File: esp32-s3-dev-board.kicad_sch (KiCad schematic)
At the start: 16 parts, among them IC1 ESP32-S3-WROOM-1-N8R8, J1 Conn_01x18, J2 Conn_01x18, J3 PROG_HDR, Q1 SS8050-G, Q2 SS8050-G, SW1 SW_Reset

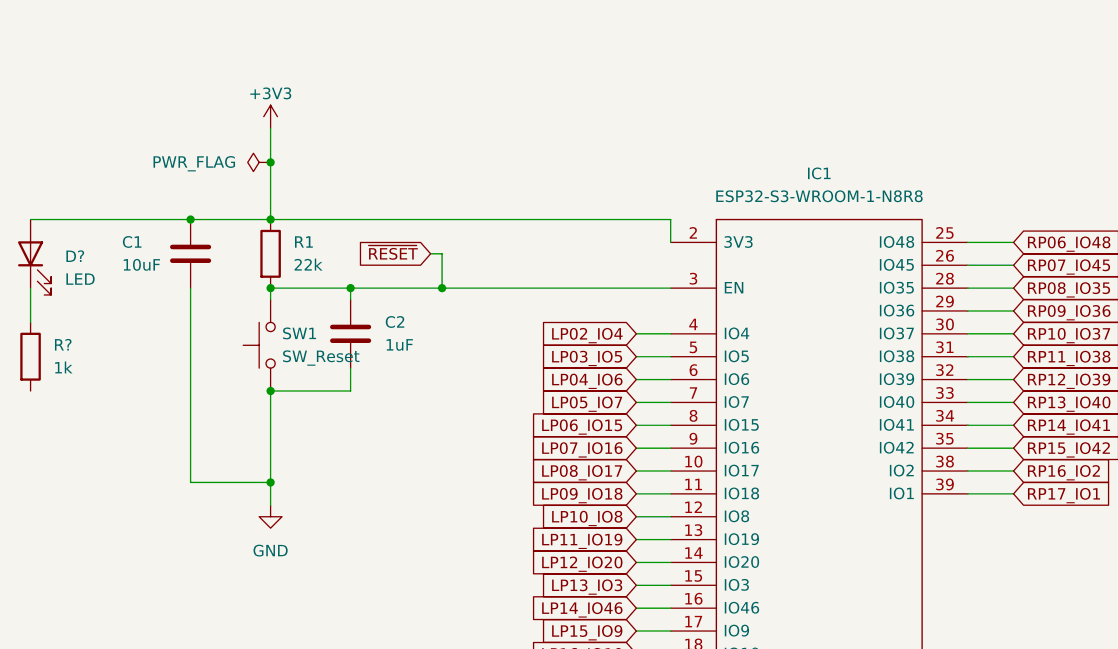
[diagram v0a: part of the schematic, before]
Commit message: Updated template for KiCAD 7
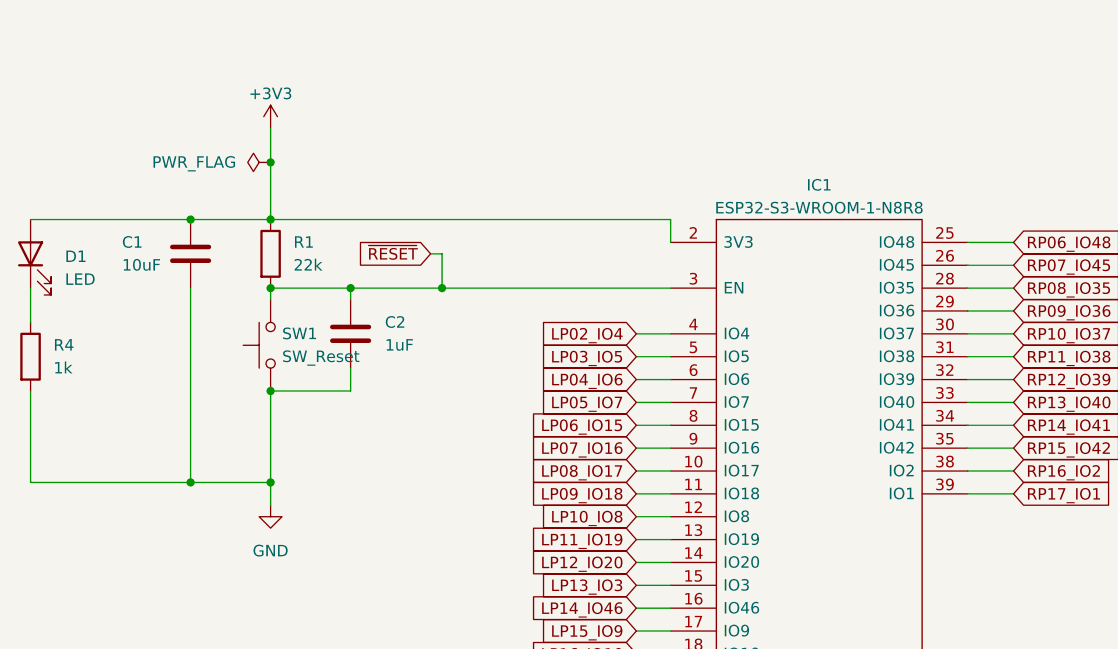
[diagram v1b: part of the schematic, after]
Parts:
- D1: renamed from D?; footprint (none) -> LED_SMD:LED_0603_1608Metric_Pad1.05x0.95mm_HandSolder
- IC1: footprint footprints:ESP32S3WROOM1N8R8 -> ESP32S3WROOM1N8R8; symbol ESP32-S3-WROOM-1-N8R8:ESP32-S3-WROOM-1-N8R8 -> MCU_Espressif:ESP32-S3-WROOM-1-N8R8
- J1, J2: footprint (none) -> Connector_PinHeader_2.54mm:PinHeader_1x18_P2.54mm_Vertical
- gave numbers to parts that had none: 1
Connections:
- net GND: now also R4.2

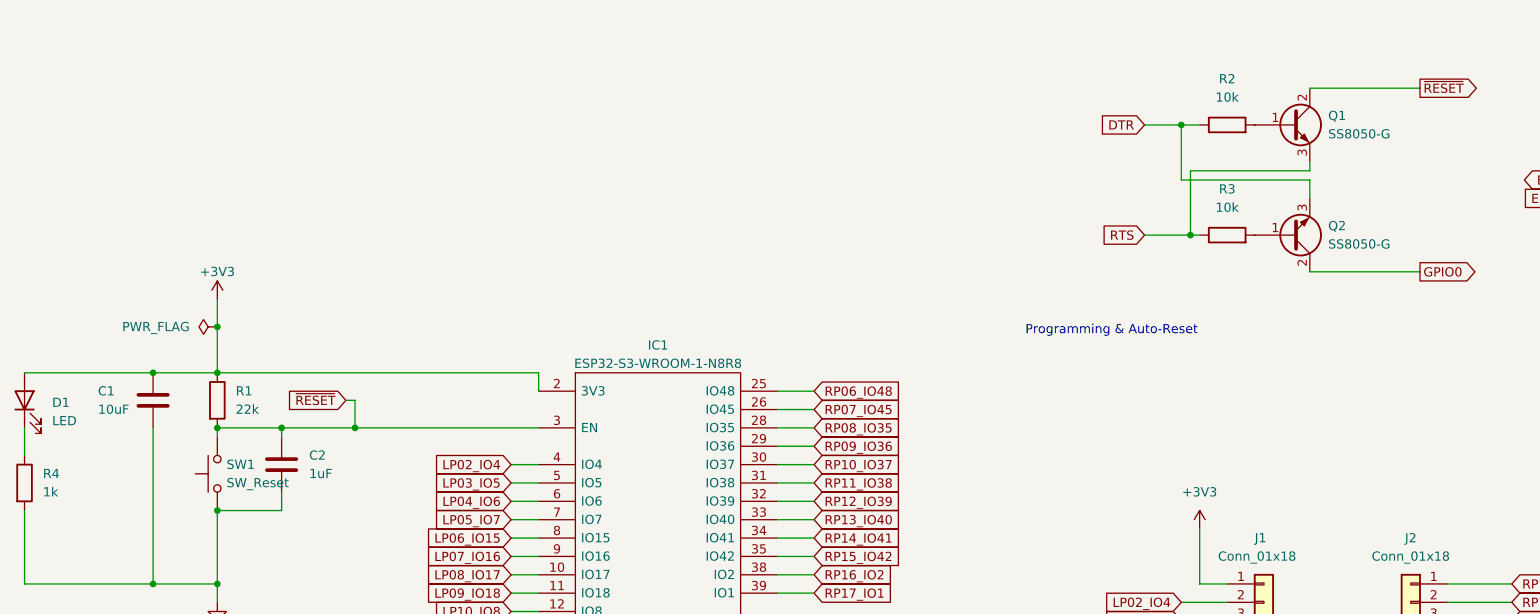
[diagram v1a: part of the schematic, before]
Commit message: Changed reset circuit to UMH3N and Upgrade to KiCad 8
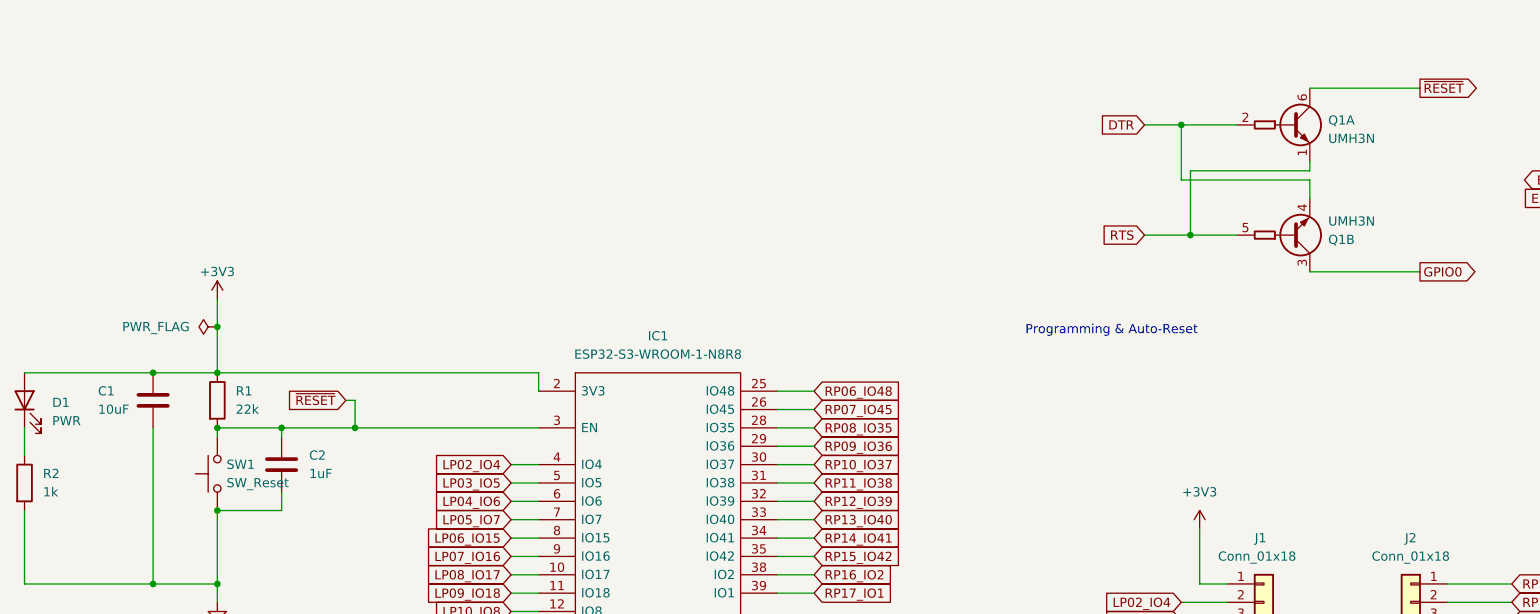
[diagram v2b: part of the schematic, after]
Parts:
- removed Q1, Q2: SS8050-G, Package_TO_SOT_SMD:SOT-23, symbol Device:Q_NPN_BCE
- removed R2, R3: 10k, Resistor_SMD:R_0603_1608Metric_Pad0.98x0.95mm_HandSolder, symbol Device:R
- added Q1: UMH3N, Package_TO_SOT_SMD:SOT-363_SC-70-6, symbol Transistor_BJT:UMH3N
- D1: value LED -> PWR
- IC1: symbol MCU_Espressif:ESP32-S3-WROOM-1-N8R8 -> Chof747 ICs:ESP32-S3-WROOM-1-N8R8
- renumbered R4 to R2
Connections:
- net  GPIO0: now also Q1.3 (C2)
- net DTR: now also Q1.2 (B1), Q1.4 (E2)
- net RTS: now also Q1.1 (E1), Q1.5 (B2)
- net ~{RESET}: now also Q1.6 (C1)

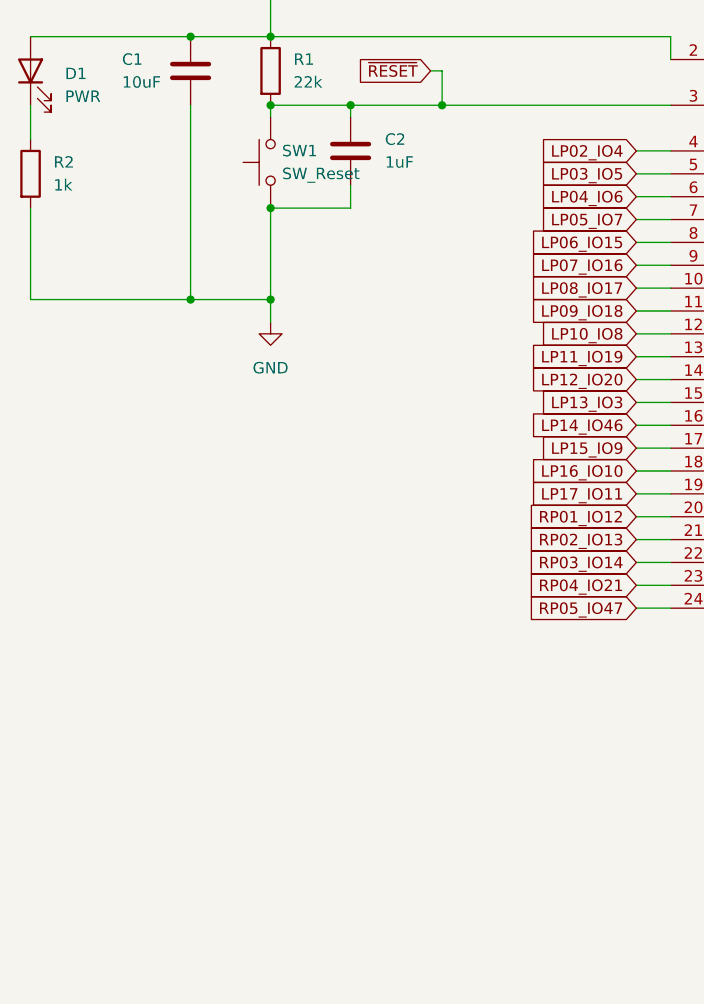
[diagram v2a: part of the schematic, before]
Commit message: Added version 1.1 with following changes:
- Changed reset and boot logic to UMH3 chip
- Added a boot button to allow manual setting into boot mode
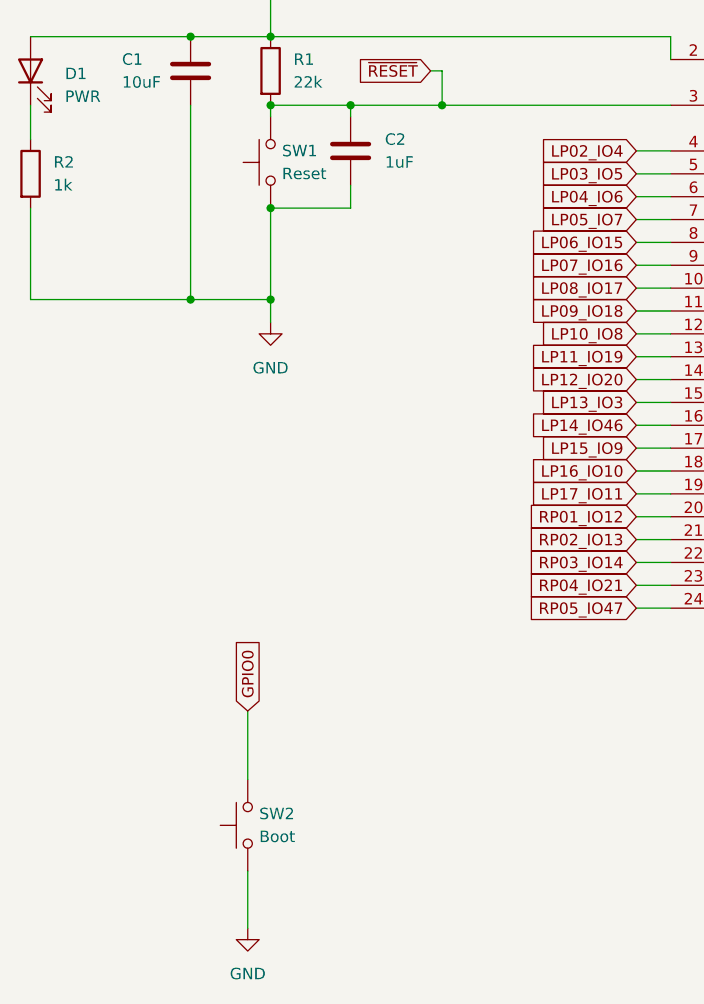
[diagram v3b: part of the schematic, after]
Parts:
- added SW2: Boot, Button_Switch_THT:SW_PUSH_6mm, symbol Switch:SW_Push
- SW1: value SW_Reset -> Reset
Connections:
- net  GPIO0: now also SW2.2
- net GND: now also SW2.1
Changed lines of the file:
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@@
 	(wire
 		(pts
+			(xy 46.99 157.48) (xy 46.99 163.83)
+		)
+		(stroke
+			(width 0)
+			(type default)
+		)
+	)
+	(wire
+		(pts
 			(xy 182.88 96.52) (xy 189.23 96.52)
 		)
@@
 	(wire
 		(pts
+			(xy 46.99 139.7) (xy 46.99 147.32)
+		)
+		(stroke
+			(width 0)
+			(type default)
+		)
+	)
+	(wire
+		(pts
 			(xy 90.17 125.73) (xy 93.98 125.73)
 		)
@@
 		)
 	)
+	(global_label " GPIO0"
+		(shape input)
+		(at 46.99 139.7 90)
+		(fields_autoplaced yes)
+		(effects
+			(font
+				(size 1.27 1.27)
+			)
+			(justify left)
+		)
+		(property "Intersheetrefs" "${INTERSHEET_REFS}"
+			(at 46.99 130.0624 90)
+			(effects
+				(font
+					(size 1.27 1.27)
+				)
+				(justify left)
+				(hide yes)
+			)
+		)
+	)
 	(global_label "RP12_IO39"
 		(shape input)
@@
 			)
 		)
-		(property "Value" "SW_Reset"
+		(property "Value" "Reset"
 			(at 50.8 80.0099 90)
 			(effects
@@
 	)
 	(symbol
+		(lib_id "Switch:SW_Push")
+		(at 46.99 152.4 90)
+		(unit 1)
+		(exclude_from_sim no)
+		(in_bom yes)
+		(on_board yes)
+		(dnp no)
+		(fields_autoplaced yes)
+		(property "Reference" "SW2"
+			(at 48.26 151.1299 90)
+			(effects
+				(font
+					(size 1.27 1.27)
+				)
+				(justify right)
+			)
+		)
+		(property "Value" "Boot"
+			(at 48.26 153.6699 90)
+			(effects
+				(font
+					(size 1.27 1.27)
+				)
+				(justify right)
+			)
+		)
+		(property "Footprint" "Button_Switch_THT:SW_PUSH_6mm"
+			(at 41.91 152.4 0)
+			(effects
+				(font
+					(size 1.27 1.27)
+				)
+				(hide yes)
+			)
+		)
+		(property "Datasheet" "~"
+			(at 41.91 152.4 0)
+			(effects
+				(font
+					(size 1.27 1.27)
+				)
+				(hide yes)
+			)
+		)
+		(property "Description" "Push button switch, generic, two pins"
+			(at 46.99 152.4 0)
+			(effects
+				(font
+					(size 1.27 1.27)
+				)
+				(hide yes)
+			)
+		)
+		(pin "1"
+		)
+		(pin "2"
+		)
+		(instances
+			(project "esp32-s3-dev-board"
+				(path "/9c0a2796-2802-493a-b118-8c7d4a430625"
+					(reference "SW2")
+					(unit 1)
+				)
+			)
+		)
+	)
+	(symbol
 		(lib_id "Jumper:Jumper_2_Open")
 		(at 240.03 26.67 0)
@@
 					(unit 1)
 				)
+			)
+		)
+	)
+	(symbol
+		(lib_id "power:GND")
+		(at 46.99 163.83 0)
+		(unit 1)
+		(exclude_from_sim no)
+		(in_bom yes)
+		(on_board yes)
+		(dnp no)
+		(property "Reference" "#PWR06"
+			(at 46.99 170.18 0)
+			(effects
+				(font
+					(size 1.27 1.27)
+				)
+				(hide yes)
+			)
+		)
+		(property "Value" "GND"
+			(at 46.99 168.91 0)
+			(effects
+				(font
+					(size 1.27 1.27)
+				)
+			)
+		)
+		(property "Footprint" ""
+			(at 46.99 163.83 0)
+			(effects
+				(font
+					(size 1.27 1.27)
+				)
+				(hide yes)
+			)
+		)
+		(property "Datasheet" ""
+			(at 46.99 163.83 0)
+			(effects
+				(font
+					(size 1.27 1.27)
+				)
+				(hide yes)
+			)
+		)
+		(property "Description" "Power symbol creates a global label with name \"GND\" , ground"
+			(at 46.99 163.83 0)
+			(effects
+				(font
+					(size 1.27 1.27)
+				)
+				(hide yes)
+			)
+		)
+		(pin "1"
+		)
+		(instances
+			(project "esp32-s3-dev-board"
+				(path "/9c0a2796-2802-493a-b118-8c7d4a430625"
+					(reference "#PWR06")
+					(unit 1)
+				)

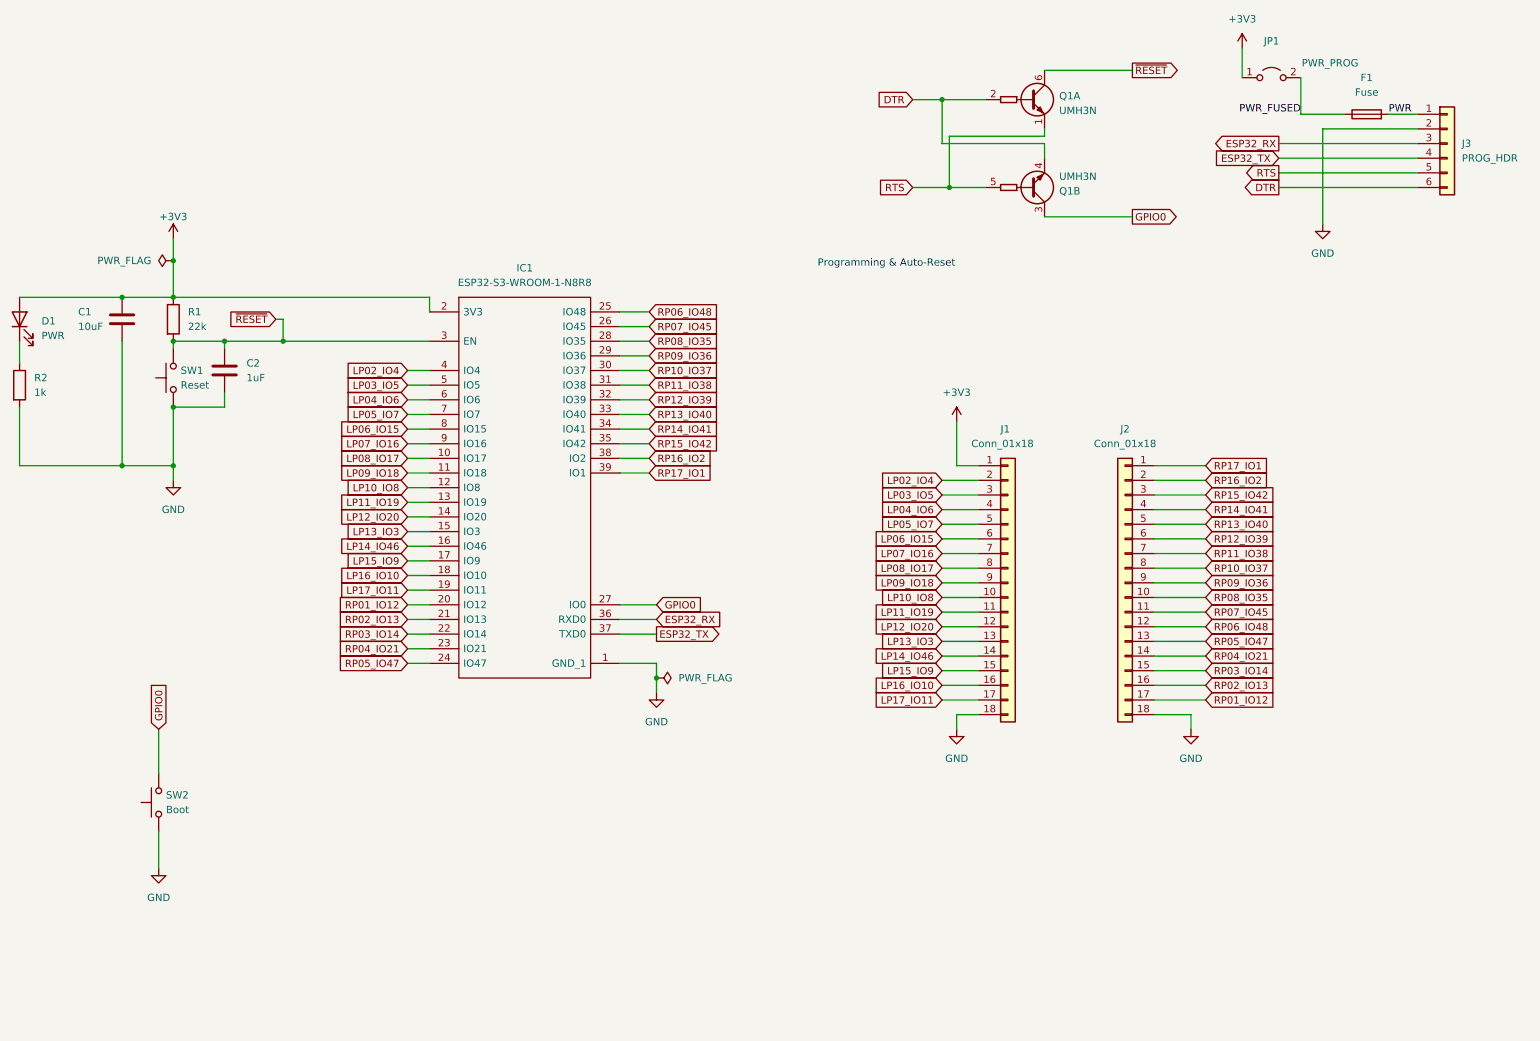
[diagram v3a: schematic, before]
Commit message: changed to slim board design - Made the board smaller so that it fits on a breadboard and leaves room for a slot on the left and right - Added a 3v3 Regulator to allow connection via an USB Breakout
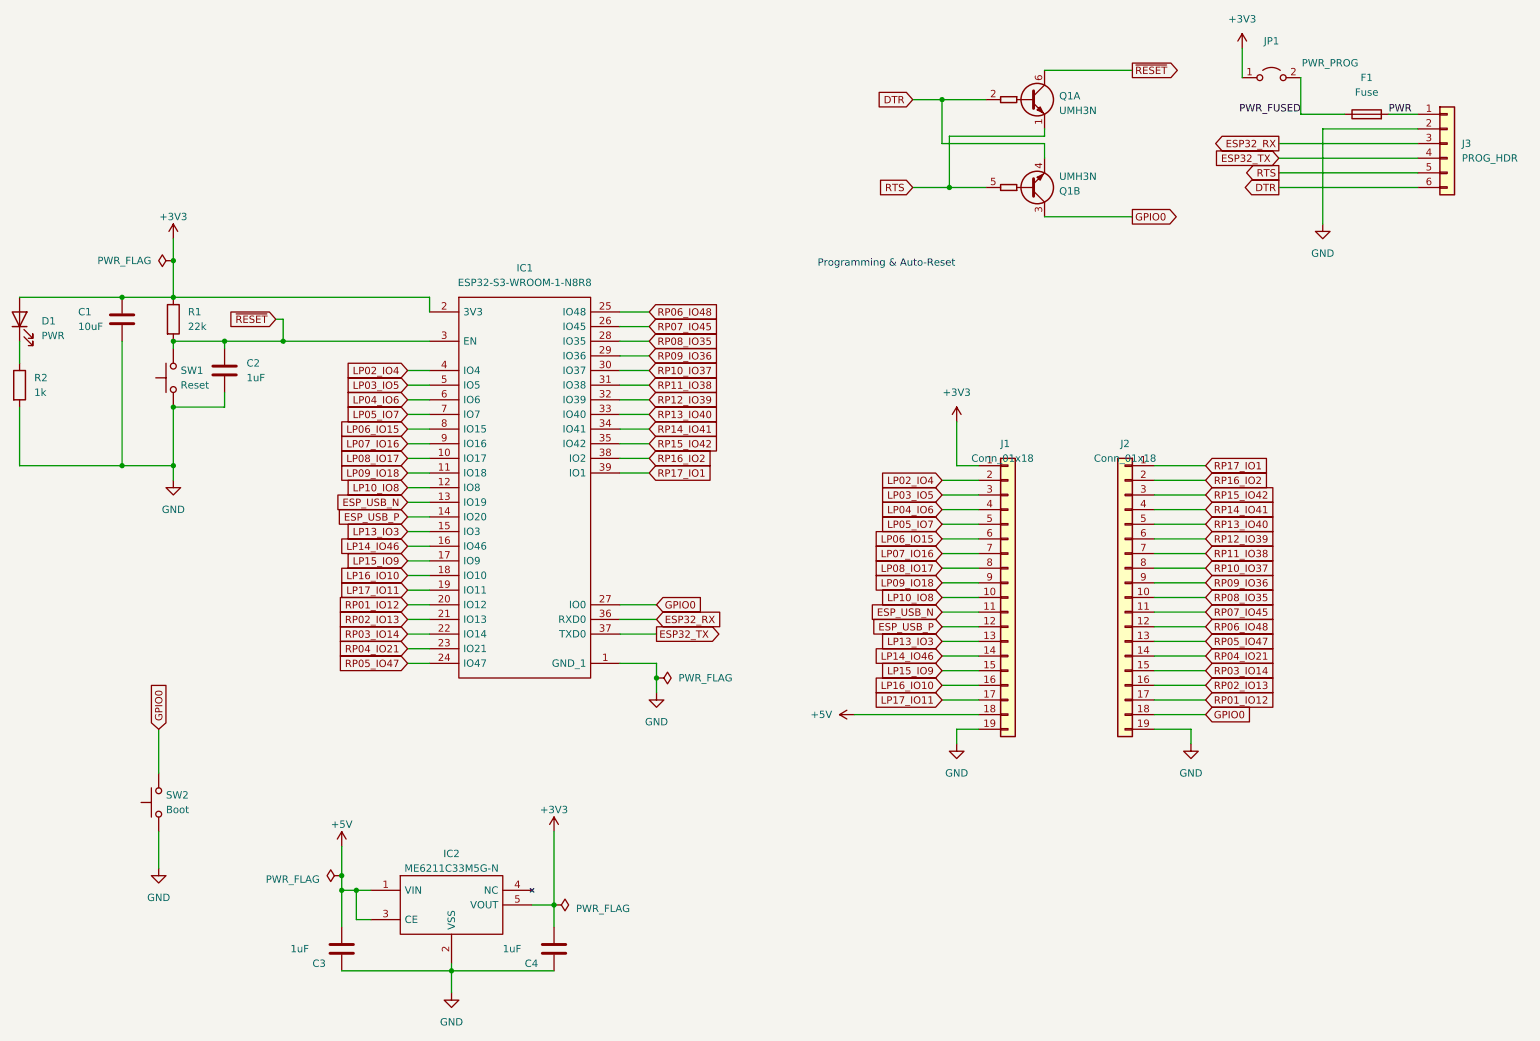
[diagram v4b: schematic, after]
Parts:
- added C3, C4: 1uF, Capacitor_SMD:C_0603_1608Metric_Pad1.08x0.95mm_HandSolder, symbol Device:C
- added IC2: ME6211C33M5G-N, SOT95P270X145-5N, symbol Chof747 Voltage Regulators:ME6211C33M5G-N
- J1, J2: footprint Connector_PinHeader_2.54mm:PinHeader_1x18_P2.54mm_Vertical -> Connector_PinHeader_2.54mm:PinHeader_1x19_P2.54mm_Vertical; symbol Connector_Generic:Conn_01x18 -> Connector_Generic:Conn_01x19
- J3: footprint Connector_PinHeader_2.54mm:PinHeader_1x06_P2.54mm_Horizontal -> Connector_PinHeader_2.54mm:PinHeader_1x06_P2.54mm_Vertical
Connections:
- net  GPIO0: now also J2.18 (Pin_18)
- net +3V3: now also C4.1, IC2.5 (VOUT)
- net GND: now also J1.19 (Pin_19), J2.19 (Pin_19), C3.2, C4.2, IC2.2 (VSS); no longer J1.18 (Pin_18), J2.18 (Pin_18)
- net LP11_IO19 renamed ESP_USB_N
- net LP12_IO20 renamed ESP_USB_P
- new net +5V: C3.1, IC2.1 (VIN), IC2.3 (CE), J1.18 (Pin_18)
